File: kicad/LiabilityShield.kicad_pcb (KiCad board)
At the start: 2 copper layers, 68.6 x 53.3 mm, 8 parts, among them P1 Power, P2 Analog, P3 Digital, P4 Digital, P5 CONN_01X01, P6 CONN_01X01, P7 CONN_01X01, P8 CONN_01X01

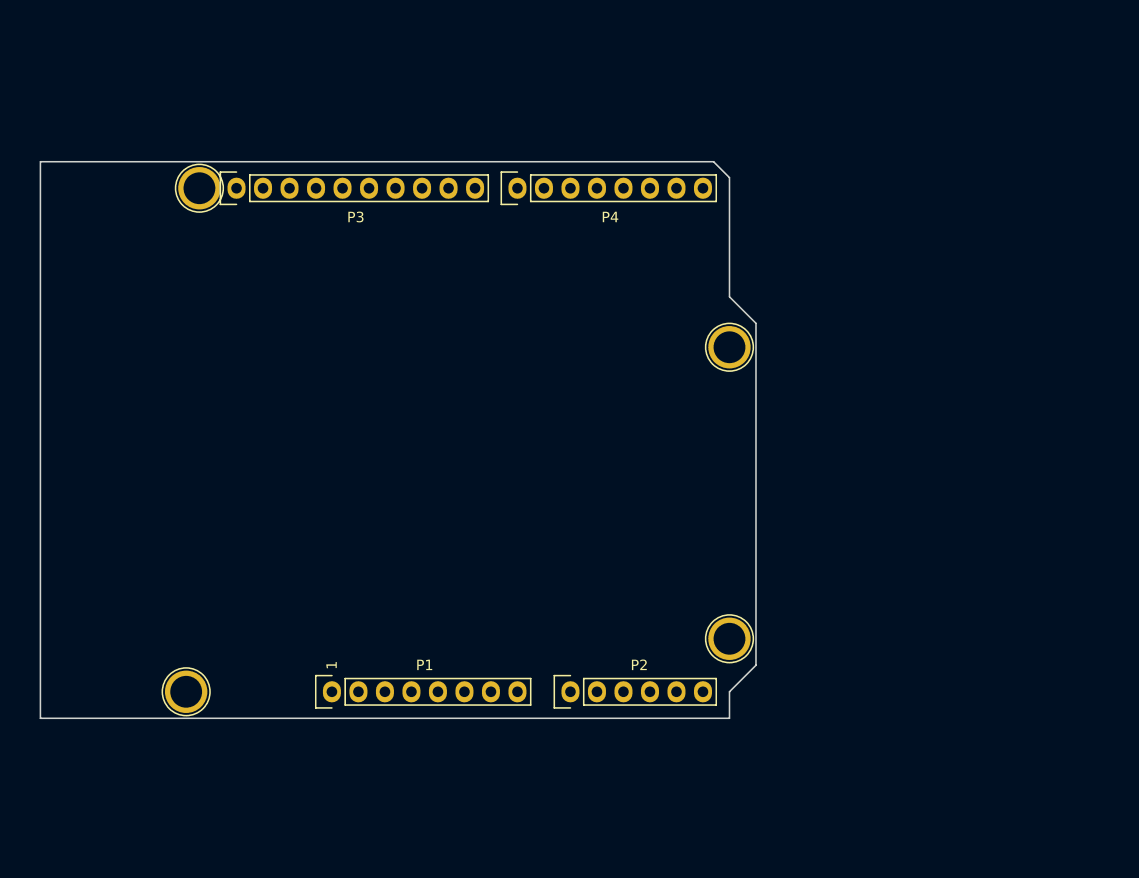
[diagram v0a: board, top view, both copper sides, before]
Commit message: Board defined
Minimal schematic and board layout
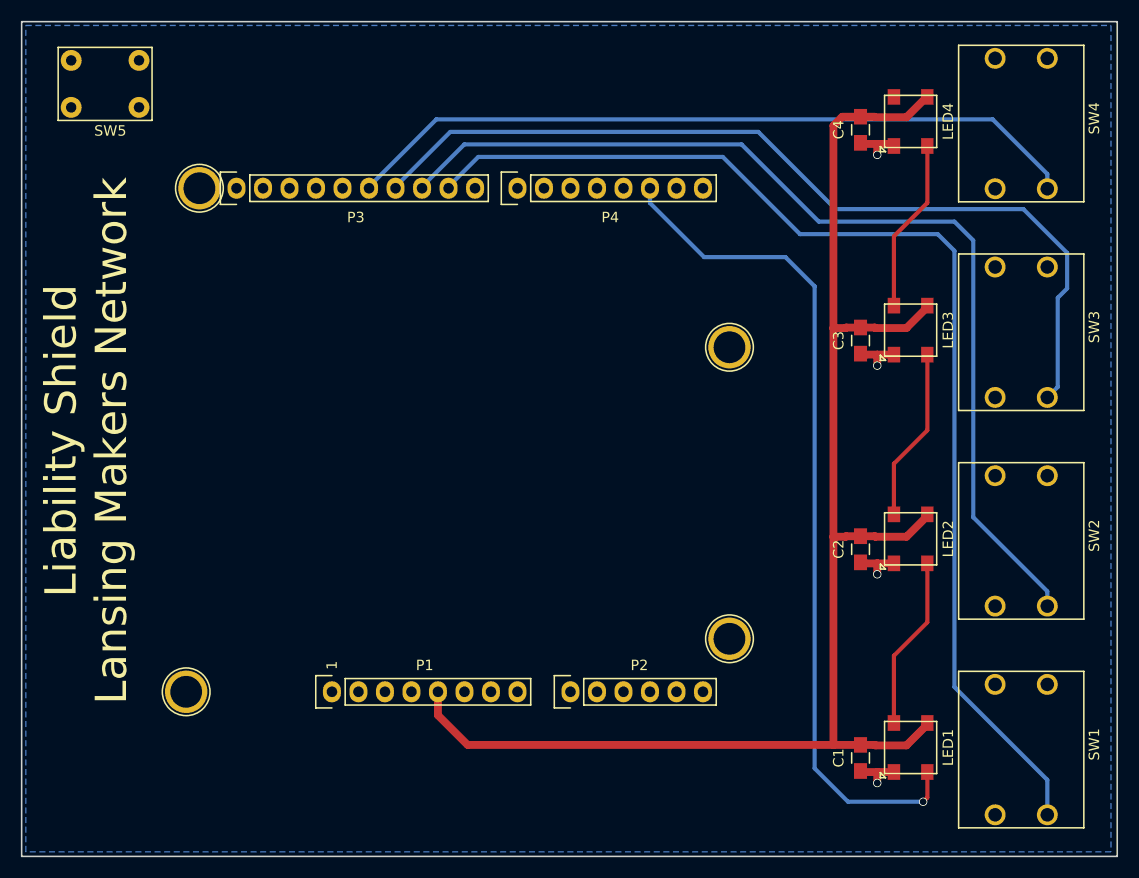
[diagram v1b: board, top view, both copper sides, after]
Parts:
- added C1: .1uF, Capacitors_SMD:C_0805_HandSoldering, F.Cu at (189.6, 130.2)
- added C2: .1uF, Capacitors_SMD:C_0805_HandSoldering, F.Cu at (189.6, 110.2)
- added C3: .1uF, Capacitors_SMD:C_0805_HandSoldering, F.Cu at (189.6, 90.2)
- added C4: .1uF, Capacitors_SMD:C_0805_HandSoldering, F.Cu at (189.6, 70.0)
- added LED1: SK6812, lib_fp:LED_5050_4pin, F.Cu at (194.4, 129.2)
- added LED2: SK6812, lib_fp:LED_5050_4pin, F.Cu at (194.4, 109.2)
- added LED3: SK6812, lib_fp:LED_5050_4pin, F.Cu at (194.4, 89.2)
- added LED4: SK6812, lib_fp:LED_5050_4pin, F.Cu at (194.4, 69.2)
- added SW1: SW_TactSwitch_4pin, lib_fp:TactSwitch_12.5_5, F.Cu at (205.0, 129.4)
- added SW2: SW_TactSwitch_4pin, lib_fp:TactSwitch_12.5_5, F.Cu at (205.0, 109.4)
- added SW3: SW_TactSwitch_4pin, lib_fp:TactSwitch_12.5_5, F.Cu at (205.0, 89.4)
- added SW4: SW_TactSwitch_4pin, lib_fp:TactSwitch_12.5_5, F.Cu at (205.0, 69.4)
- added SW5: SW_Push, lib_fp:TactSwitch_6.5_4.5, F.Cu at (117.2, 65.6)
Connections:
- net /0(Rx) renamed /D0(Rx)
- net /1(Tx) renamed /D1(Tx)
- net /13(SCK) renamed /D13(SCK)
- net /3(**) renamed /D3(**)
- net /4 renamed /D4
- net /5(**) renamed /D5(**)
- net /6(**) renamed /D6(**)
- net /7 renamed /D7
- net /8 renamed /D8
- P3 pad 6: /12(MISO) -> /D12(MISO)
- P3 pad 7: /11(**/MOSI) -> /D11(**/MOSI)
- P3 pad 8: /10(**/SS) -> /D10(**/SS)
- P3 pad 9: /9(**) -> /D9(**)
- P4 pad 6: /2 -> /D2
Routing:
- net +5V: track 0.00 -> 140.8 mm
- net /D9(**): track 0.00 -> 111.3 mm
- net /D10(**/SS): track 0.00 -> 96.5 mm
- net /D11(**/MOSI): track 0.00 -> 86.1 mm
- net /D2: track 0.00 -> 81.4 mm, vias 0 -> 1
- net /D12(MISO): track 0.00 -> 71.4 mm
- net GND: track 0.00 -> 16.9 mm, vias 0 -> 4
- net Net-(LED1-Pad4): track 0.00 -> 16.6 mm
- net Net-(LED3-Pad4): track 0.00 -> 16.6 mm
- net Net-(LED2-Pad4): track 0.00 -> 16.6 mm
- added copper zone on B.Cu, net GND
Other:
- board size 68.6 x 53.3 mm -> 105 x 80 mm
- rule trace_min: 0.2 -> 0.1524
- rule via_min_drill: 0.3 -> 0.254
- rule via_min_size: 0.4 -> 0.508
- board text added: "Liability Shield Lansing Makers Network"
